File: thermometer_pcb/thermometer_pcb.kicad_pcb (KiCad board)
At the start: 2 copper layers, 76.6 x 49 mm, 19 parts, among them J1 POWER_IN, J2 TC_IN, J3 EXT_DS1, J4 EXT_DS2, J5 DISP, J6 Conn_01x02, J7 SPI, Q1 PN2222A, U1 DS18B20

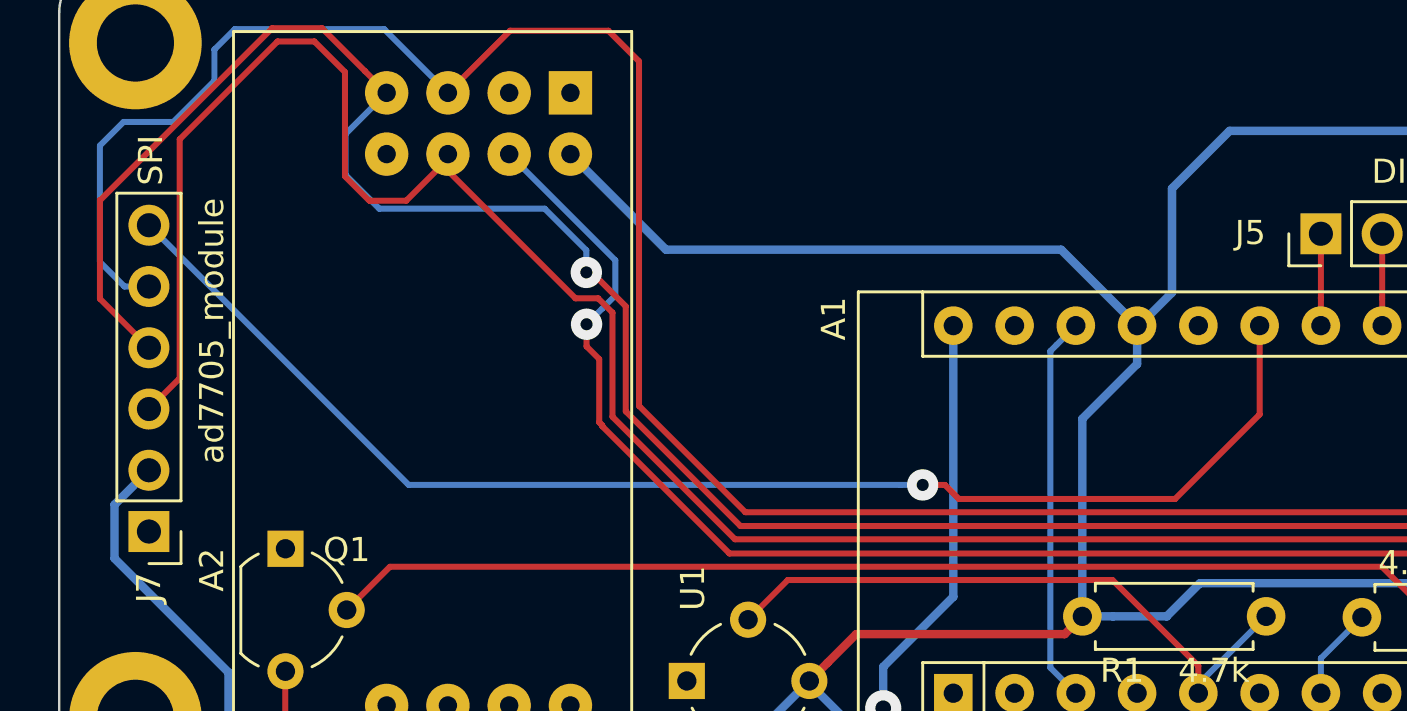
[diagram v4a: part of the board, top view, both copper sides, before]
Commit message: pcb: add buzzer
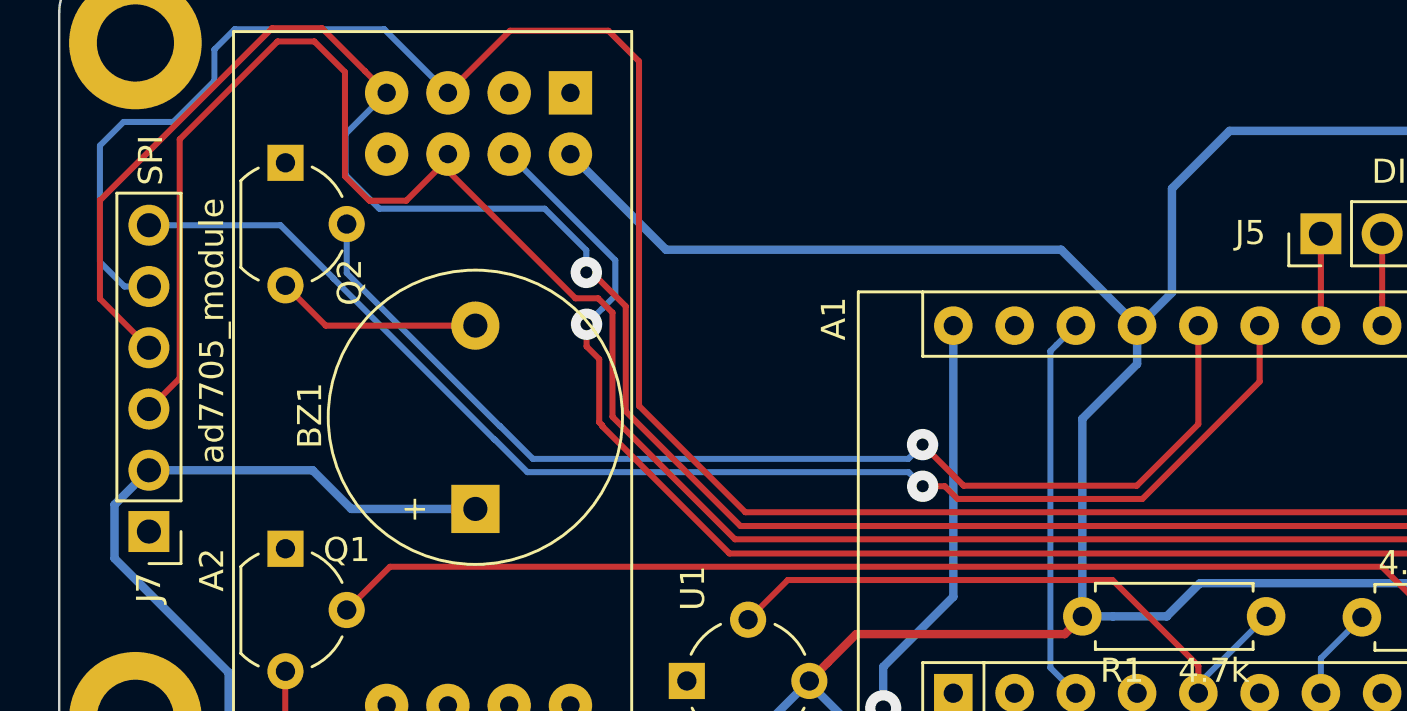
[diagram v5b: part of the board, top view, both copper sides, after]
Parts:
- added BZ1: Buzzer, Buzzer_Beeper:Buzzer_12x9.5RM7.6, F.Cu at (162.9, 66.6)
- added Q2: PN2222A, Package_TO_SOT_THT:TO-92_Wide, F.Cu at (155.0, 52.3)
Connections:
- A1 pad 26: (no net) -> /A7
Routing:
- net /A7: track 0.00 -> 46.6 mm, vias 0 -> 1
- net +5V: track 195.0 -> 209.2 mm
- net Net-(BZ1-Pad2): track 0.00 -> 8.57 mm
- net /A6: track 55.9 -> 55.1 mm

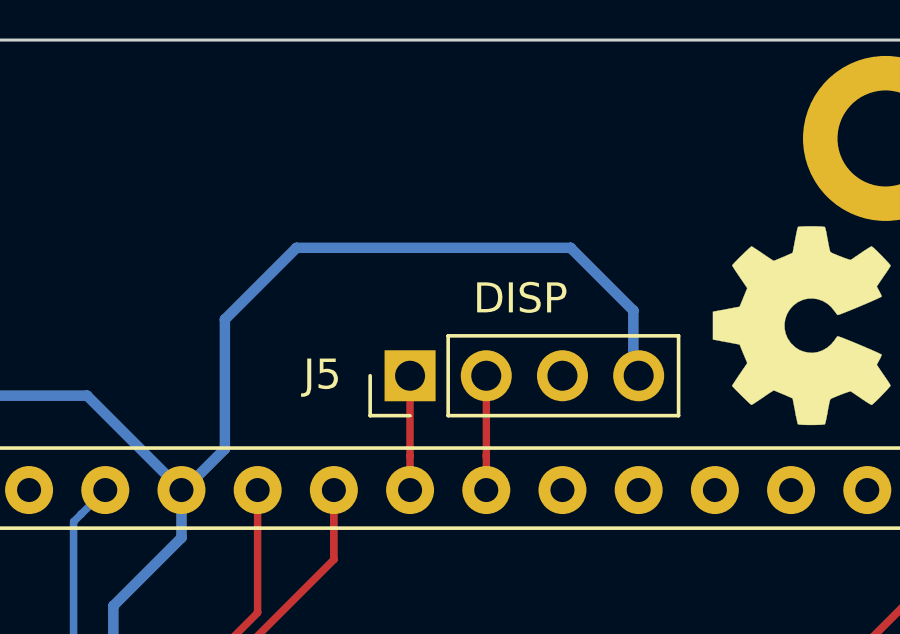
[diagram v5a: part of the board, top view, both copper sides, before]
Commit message: pcb: add I2C pinheader
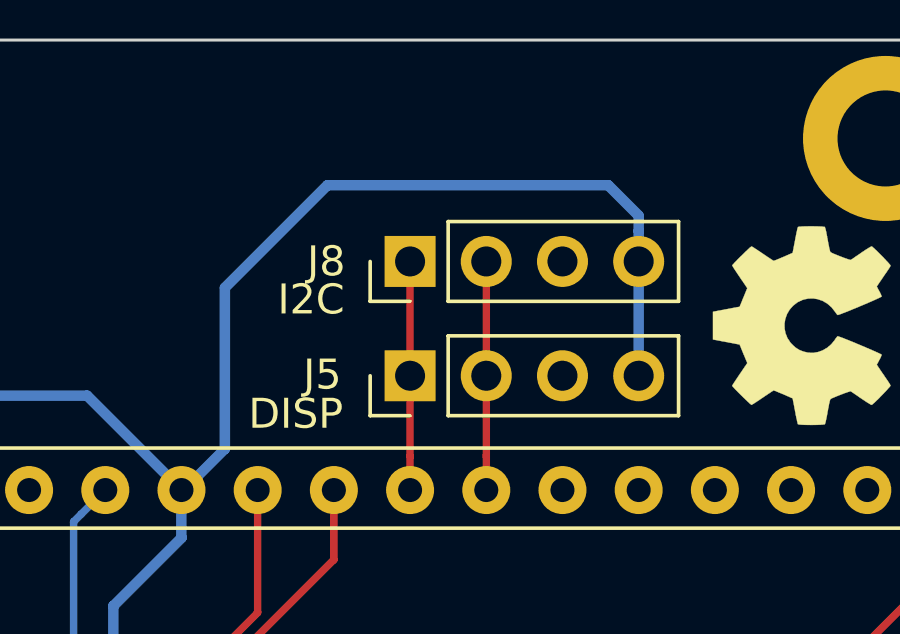
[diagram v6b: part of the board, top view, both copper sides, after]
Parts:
- added J8: I2C, Connector_PinHeader_2.54mm:PinHeader_1x04_P2.54mm_Vertical, F.Cu at (197.9, 51.4)
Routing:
- net +5V: track 209.2 -> 213.5 mm
- net /A5: track 3.81 -> 7.62 mm
- net /A4: track 3.81 -> 7.62 mm
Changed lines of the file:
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@@
     (thickness 1.6)
     (drawings 60)
-    (tracks 198)
-    (modules 21)
+    (tracks 201)
+    (modules 22)
     (nets 23)
   )
@@
     (solder_mask_min_width 0.25)
     (aux_axis_origin 139.446 106.807)
-    (grid_origin 155.017557 68.268844)
+    (grid_origin 197.948677 55.208604)
     (visible_elements FFFFF77F)
     (pcbplotparams
@@
     (uvia_dia 0.7)
     (uvia_drill 0.3)
+  )
+  (module "Connector_PinHeader_2.54mm:PinHeader_1x04_P2.54mm_Vertical" (layer "F.Cu")
+    (at 197.948677 51.398604 90)
+    (descr "Through hole straight pin header, 1x04, 2.54mm pitch, single row")
+    (tags "Through hole pin header THT 1x04 2.54mm single row")
+    (fp_text reference "J8" (at 0 -2.794 180) (layer "F.SilkS")
+      (effects (font (size 1 1) (thickness 0.15)))
+    )
+    (fp_text value "I2C" (at -1.27 -3.302 180) (layer "F.SilkS")
+      (effects (font (size 1 1) (thickness 0.15)))
+    )
+    (fp_line (start -0.635 -1.27) (end 1.27 -1.27) (layer "F.Fab") (width 0.1))
+    (fp_line (start 1.27 -1.27) (end 1.27 8.89) (layer "F.Fab") (width 0.1))
+    (fp_line (start 1.27 8.89) (end -1.27 8.89) (layer "F.Fab") (width 0.1))
+    (fp_line (start -1.27 8.89) (end -1.27 -0.635) (layer "F.Fab") (width 0.1))
+    (fp_line (start -1.27 -0.635) (end -0.635 -1.27) (layer "F.Fab") (width 0.1))
+    (fp_line (start -1.33 8.95) (end 1.33 8.95) (layer "F.SilkS") (width 0.12))
+    (fp_line (start -1.33 1.27) (end -1.33 8.95) (layer "F.SilkS") (width 0.12))
+    (fp_line (start 1.33 1.27) (end 1.33 8.95) (layer "F.SilkS") (width 0.12))
+    (fp_line (start -1.33 1.27) (end 1.33 1.27) (layer "F.SilkS") (width 0.12))
+    (fp_line (start -1.33 0) (end -1.33 -1.33) (layer "F.SilkS") (width 0.12))
+    (fp_line (start -1.33 -1.33) (end 0 -1.33) (layer "F.SilkS") (width 0.12))
+    (fp_line (start -1.8 -1.8) (end -1.8 9.4) (layer "F.CrtYd") (width 0.05))
+    (fp_line (start -1.8 9.4) (end 1.8 9.4) (layer "F.CrtYd") (width 0.05))
+    (fp_line (start 1.8 9.4) (end 1.8 -1.8) (layer "F.CrtYd") (width 0.05))
+    (fp_line (start 1.8 -1.8) (end -1.8 -1.8) (layer "F.CrtYd") (width 0.05))
+    (fp_text user "%R" (at 0 3.81) (layer "F.Fab")
+      (effects (font (size 1 1) (thickness 0.15)))
+    )
+    (pad "4" thru_hole oval (at 0 7.62 90) (size 1.7 1.7) (drill 1) (layers *.Cu *.Mask)
+      (net 2 "+5V"))
+    (pad "3" thru_hole oval (at 0 5.08 90) (size 1.7 1.7) (drill 1) (layers *.Cu *.Mask)
+      (net 1 "GND"))
+    (pad "2" thru_hole oval (at 0 2.54 90) (size 1.7 1.7) (drill 1) (layers *.Cu *.Mask)
+      (net 11 "/A4"))
+    (pad "1" thru_hole rect (at 0 0 90) (size 1.7 1.7) (drill 1) (layers *.Cu *.Mask)
+      (net 10 "/A5"))
+    (model "${KISYS3DMOD}/Connector_PinHeader_2.54mm.3dshapes/PinHeader_1x04_P2.54mm_Vertical.wrl"
+      (at (xyz 0 0 0))
+      (scale (xyz 1 1 1))
+      (rotate (xyz 0 0 0))
+    )
   )
   (module "Package_TO_SOT_THT:TO-92_Wide" (layer "F.Cu")
@@
       (effects (font (size 1 1) (thickness 0.15)))
     )
-    (fp_text value "DISP" (at 2.576 3.679999 180) (layer "F.SilkS")
+    (fp_text value "DISP" (at -1.27 -3.81 180) (layer "F.SilkS")
       (effects (font (size 1 1) (thickness 0.15)))
     )
@@
   (gr_line (start 222.221676 76.190177) (end 222.221676 46.018604) (layer "Edge.Cuts") (width 0.1))
   (gr_arc (start 220.221676 46.018604) (end 222.221676 46.018604) (angle -90) (layer "Edge.Cuts") (width 0.1))
+  (segment (start 197.948677 55.208604) (end 197.948677 51.398604) (width 0.25) (layer "F.Cu") (net 10))
+  (segment (start 200.488677 55.208604) (end 200.488677 51.398604) (width 0.25) (layer "F.Cu") (net 11))
+  (segment (start 195.193177 48.858604) (end 204.552677 48.858604) (width 0.35) (layer "B.Cu") (net 2))
+  (segment (start 191.775177 52.276604) (end 195.193177 48.858604) (width 0.35) (layer "B.Cu") (net 2))
+  (segment (start 191.775177 57.649104) (end 191.775177 52.276604) (width 0.35) (layer "B.Cu") (net 2))
+  (segment (start 190.405677 59.018604) (end 191.775177 57.649104) (width 0.35) (layer "B.Cu") (net 2))
+  (segment (start 190.328677 59.018604) (end 190.405677 59.018604) (width 0.35) (layer "B.Cu") (net 2))
+  (segment (start 204.552677 48.858604) (end 205.568677 49.874604) (width 0.35) (layer "B.Cu") (net 2))
+  (segment (start 205.568677 49.874604) (end 205.568677 50.382604) (width 0.35) (layer "B.Cu") (net 2))
+  (segment (start 205.568677 50.382604) (end 205.568677 51.398604) (width 0.35) (layer "B.Cu") (net 2))
+  (segment (start 205.568677 51.398604) (end 205.568677 55.208604) (width 0.35) (layer "B.Cu") (net 2))
   (segment (start 163.923386 63.188842) (end 165.278377 64.543834) (width 0.25) (layer "B.Cu") (net 20))
   (segment (start 157.557557 54.806844) (end 157.557557 56.838844) (width 0.25) (layer "B.Cu") (net 20))
@@
   (segment (start 189.307058 69.565615) (end 192.868677 73.127234) (width 0.25) (layer "F.Cu") (net 13))
   (segment (start 192.868677 73.127234) (end 192.868677 74.258604) (width 0.25) (layer "F.Cu") (net 13))
-  (segment (start 194.162777 50.943504) (end 203.297877 50.943504) (width 0.35) (layer "B.Cu") (net 2))
-  (segment (start 205.393377 53.039004) (end 205.393377 55.033304) (width 0.35) (layer "B.Cu") (net 2))
-  (segment (start 191.775177 53.331104) (end 194.162777 50.943504) (width 0.35) (layer "B.Cu") (net 2))
-  (segment (start 190.328677 59.018604) (end 190.405677 59.018604) (width 0.35) (layer "B.Cu") (net 2))
-  (segment (start 191.775177 57.649104) (end 191.775177 53.331104) (width 0.35) (layer "B.Cu") (net 2))
-  (segment (start 203.297877 50.943504) (end 205.393377 53.039004) (width 0.35) (layer "B.Cu") (net 2))
-  (segment (start 190.405677 59.018604) (end 191.775177 57.649104) (width 0.35) (layer "B.Cu") (net 2))
-  (segment (start 205.393377 55.033304) (end 205.568677 55.208604) (width 0.35) (layer "B.Cu") (net 2))
   (segment (start 205.856076 69.698003) (end 192.934278 69.698003) (width 0.35) (layer "B.Cu") (net 2))
   (segment (start 207.269177 71.111104) (end 205.856076 69.698003) (width 0.35) (layer "B.Cu") (net 2))

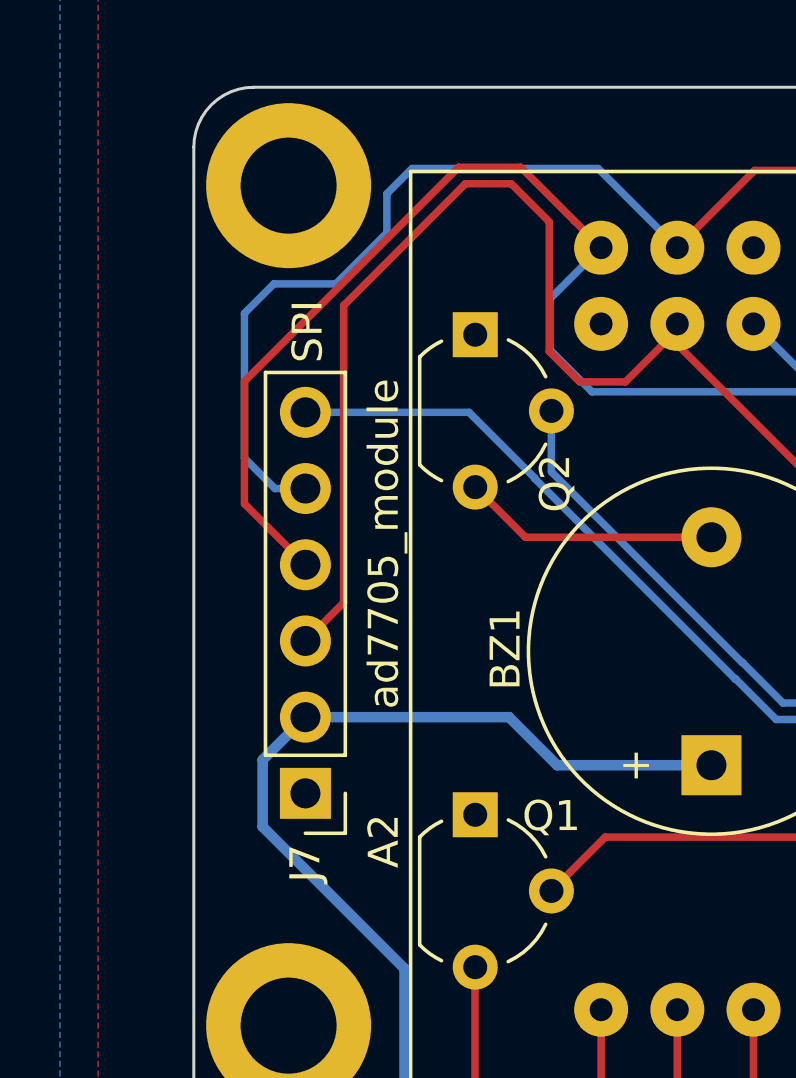
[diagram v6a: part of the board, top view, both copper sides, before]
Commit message: pcb: add SPI pins silkscreen
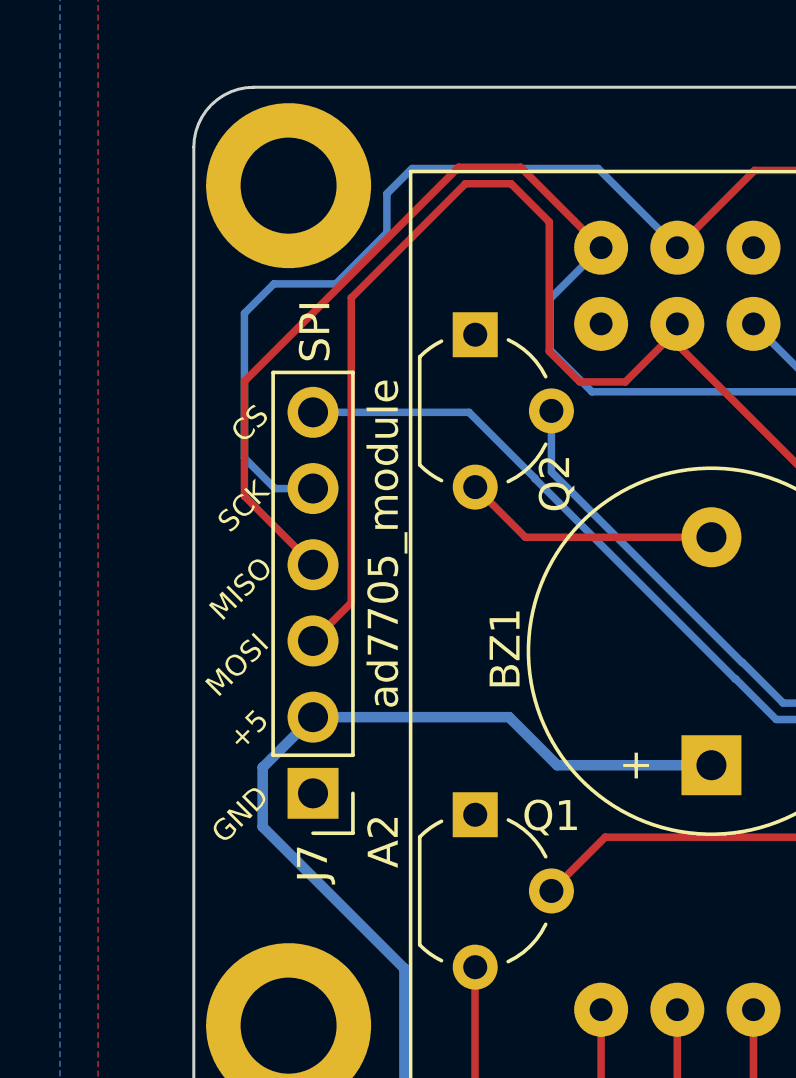
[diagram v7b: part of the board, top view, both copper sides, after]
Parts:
- moved J7 0.25 mm to (149.6, 67.6)
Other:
- board text added: "CS"
- board text added: "MISO"
- board text added: "MOSI"
- board text added: "SCK"
